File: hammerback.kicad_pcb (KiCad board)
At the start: 2 copper layers, 20.8 x 8.6 mm, 47 parts, among them J1 USB_C_Receptacle_USB2.0, P1 USB_C_Plug_USB2.0, U1 MCP73871, U2 TPS61090

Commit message: R0
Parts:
- removed BT1: Battery, KiCad/Connector_JST.pretty:JST_PH_S2B-PH-SM4-TB_1x02-1MP_P2.00mm_Horizontal
- removed F1: 3 A, KiCad/Capacitor_SMD.pretty:C_1206_3216Metric_Pad1.42x1.75mm_HandSolder
- removed REF** (x2): MountingHole_2.7mm_M2.5_ISO7380, KiCad/MountingHole.pretty:MountingHole_2.7mm_M2.5_ISO7380
- removed TH1: 10k, KiCad/Connector_PinHeader_2.54mm.pretty:PinHeader_1x02_P2.54mm_Vertical
- removed TP10, TP11, TP12, TP5, TP6, TP7, TP8, TP9: TestPoint, KiCad/TestPoint.pretty:TestPoint_Pad_D1.5mm
- added G***: LOGO, tunaf1sh/JBR-logos.pretty:hammerback, B.Cu at (155.3, 101.5)
- added G***: LOGO, tunaf1sh/JBR-logos.pretty:jbr-binary-xs-mask, B.Cu at (166.4, 100.2)
- added H1: MountingHole, KiCad/MountingHole.pretty:MountingHole_3.2mm_M3_ISO14580, F.Cu at (135.8, 95.7)
- added H2: MountingHole, KiCad/MountingHole.pretty:MountingHole_3.2mm_M3_ISO14580, F.Cu at (165.8, 95.7)
- added J2: LiPo, KiCad/Connector_PinHeader_2.54mm.pretty:PinHeader_1x03_P2.54mm_Vertical, F.Cu at (144.3, 97.7)
- JP1, R8, R9, TP3: moved to B.Cu
- TP1, TP2: value TestPoint_Probe -> TestPoint; footprint KiCad/TestPoint.pretty:TestPoint_Keystone_5019_Minature -> KiCad/TestPoint.pretty:TestPoint_Pad_D1.5mm
- moved C4 57.9 mm to (153.8, 98.7), turned to 180 degrees
- moved JP1 54.2 mm to (146.3, 101.7), turned to 90 degrees
- moved TP4 53.4 mm to (158.4, 98.3), turned to 90 degrees
- moved C1 51.5 mm to (146.6, 92.6)
- moved L1 50.2 mm to (155.3, 104.0), turned to 90 degrees
- moved TP3 45.7 mm to (150.9, 104.3)
- moved C5 44.7 mm to (166.7, 104.7)
- moved D1 44.7 mm to (144.3, 107.0)
- moved D2 44.7 mm to (142.6, 107.0)
- moved R1 44.7 mm to (148.9, 107.0)
- moved R10 44.7 mm to (141.1, 107.0)
- moved R2 44.7 mm to (147.4, 107.0)
- moved R7 44.7 mm to (145.8, 107.0)
- moved U1 44.6 mm to (148.3, 102.2)
- moved U2 44.4 mm to (162.0, 101.9), turned to 270 degrees
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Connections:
- net Net-(R5-Pad2) renamed /NTC
- TP1 pad 1: (no net) -> GND
- TP2 pad 1: GND -> VBUS
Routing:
- net GND: track 65.0 -> 114.0 mm, vias 6 -> 8
- net VBUS: track 7.46 -> 52.5 mm, vias 1 -> 4
- net /USB_N: track 4.81 -> 30.1 mm, vias 0 -> 3
- net /USB_P: track 7.58 -> 29.2 mm, vias 0 -> 3
- net VDD: track 15.4 -> 0.00 mm, vias 2 -> 0
- net Net-(BT1-Pad1): track 10.6 -> 0.00 mm
- net Net-(R16-Pad2): track 0.00 -> 9.82 mm
- net Net-(P1-PadB5): track 2.83 -> 12.0 mm
- net /NTC: track 4.63 -> 9.08 mm
- net Net-(P1-PadA5): track 4.49 -> 8.32 mm
- net Net-(C2-Pad1): track 29.5 -> 33.3 mm
- net Net-(C1-Pad1): track 24.3 -> 21.4 mm, vias 2 -> 1
- net Net-(J1-PadB5): track 0.00 -> 2.03 mm, vias 0 -> 1
- net Net-(J1-PadA5): track 0.00 -> 2.02 mm, vias 0 -> 1
- net +5V: track 30.1 -> 31.9 mm
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- added copper zone on B.Cu, net GND
- added copper zone on F.Cu, net GND
- removed copper zone on B.Cu, net (none)
- removed copper zone on F.Cu, net (none)
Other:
- board size 20.8 x 8.6 mm -> 36 x 18 mm
- board text added: "Hammerback R0 JBR Engineering 2021"
- board text removed: "+"
- board text removed: "-"
- board text removed: "2. VBATT- 1. VBATT+"
- board text removed: "5V"
- board text removed: "C1"
- board text removed: "C2"
- board text removed: "USB-C Plug"

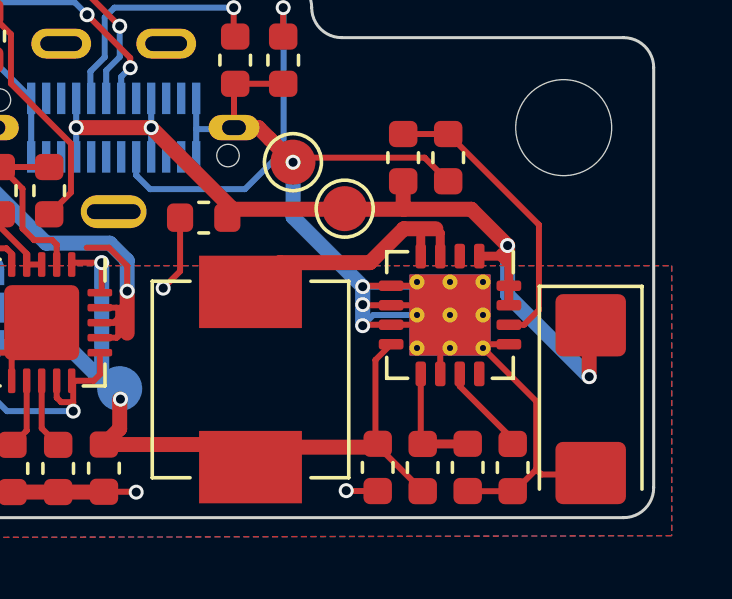
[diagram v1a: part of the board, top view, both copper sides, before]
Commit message: fix hole size in pad
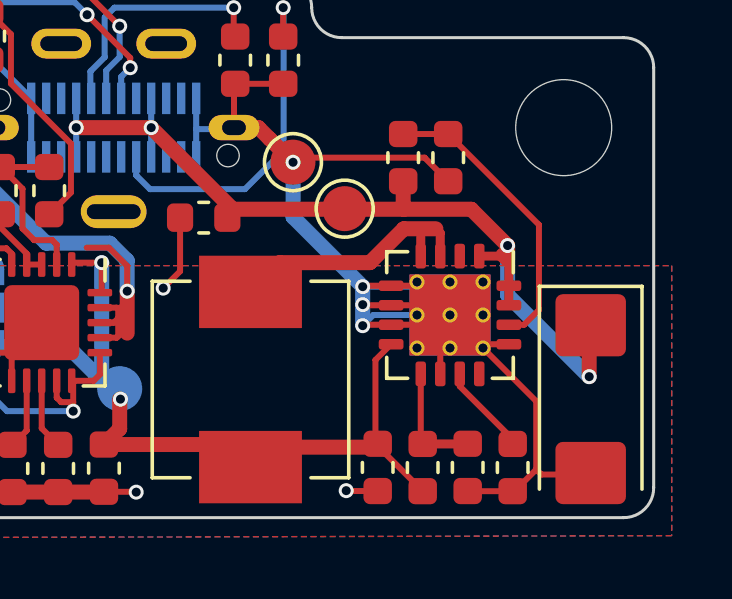
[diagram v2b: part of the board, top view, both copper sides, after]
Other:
- rule via_min_size: 0.5 -> 0.3
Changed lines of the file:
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@@
   )
   (setup
-    (last_trace_width 0.5)
+    (last_trace_width 0.2)
     (user_trace_width 0.3)
     (user_trace_width 0.5)
@@
     (via_size 0.5)
     (via_drill 0.3)
-    (via_min_size 0.5)
+    (via_min_size 0.3)
     (via_min_drill 0.3)
     (user_via 0.6 0.4)
@@
     (diff_pair_gap 0.15)
   )
-  (module KiCad/Capacitor_Tantalum_SMD.pretty:CP_EIA-6032-20_AVX-F (layer F.Cu)
-    (at 166.65 104.7 270)
-    (descr "Tantalum Capacitor SMD AVX-F (6032-20 Metric), IPC_7351 nominal, (Body size from: http://www.kemet.com/Lists/ProductCatalog/Attachments/253/KEM_TC101_STD.pdf), generated with kicad-footprint-generator")
-    (tags "capacitor tantalum")
-    (attr smd)
-    (fp_text reference C5 (at 0 -2.55 90) (layer F.SilkS) hide
-      (effects (font (size 1 1) (thickness 0.15)))
-    )
-    (fp_text value 100u (at 0 2.55 90) (layer F.Fab)
-      (effects (font (size 1 1) (thickness 0.15)))
-    )
-    (fp_line (start 3.75 1.85) (end -3.75 1.85) (layer F.CrtYd) (width 0.05))
-    (fp_line (start 3.75 -1.85) (end 3.75 1.85) (layer F.CrtYd) (width 0.05))
-    (fp_line (start -3.75 -1.85) (end 3.75 -1.85) (layer F.CrtYd) (width 0.05))
-    (fp_line (start -3.75 1.85) (end -3.75 -1.85) (layer F.CrtYd) (width 0.05))
-    (fp_line (start -3.76 1.71) (end 3 1.71) (layer F.SilkS) (width 0.12))
-    (fp_line (start -3.76 -1.71) (end -3.76 1.71) (layer F.SilkS) (width 0.12))
-    (fp_line (start 3 -1.71) (end -3.76 -1.71) (layer F.SilkS) (width 0.12))
-    (fp_line (start 3 1.6) (end 3 -1.6) (layer F.Fab) (width 0.1))
-    (fp_line (start -3 1.6) (end 3 1.6) (layer F.Fab) (width 0.1))
-    (fp_line (start -3 -0.8) (end -3 1.6) (layer F.Fab) (width 0.1))
-    (fp_line (start -2.2 -1.6) (end -3 -0.8) (layer F.Fab) (width 0.1))
-    (fp_line (start 3 -1.6) (end -2.2 -1.6) (layer F.Fab) (width 0.1))
-    (fp_text user %R (at 0 0 90) (layer F.Fab)
-      (effects (font (size 1 1) (thickness 0.15)))
-    )
-    (pad 2 smd roundrect (at 2.4625 0 270) (size 2.075 2.35) (layers F.Cu F.Paste F.Mask) (roundrect_rratio 0.1204819277108434)
-      (net 2 GND))
-    (pad 1 smd roundrect (at -2.4625 0 270) (size 2.075 2.35) (layers F.Cu F.Paste F.Mask) (roundrect_rratio 0.1204819277108434)
-      (net 5 +5V))
-    (model ${KISYS3DMOD}/Capacitor_Tantalum_SMD.3dshapes/CP_EIA-6032-20_AVX-F.wrl
-      (at (xyz 0 0 0))
-      (scale (xyz 1 1 1))
-      (rotate (xyz 0 0 0))
-    )
-  )
-  (module KiCad/MountingHole.pretty:MountingHole_3.2mm_M3_ISO14580 (layer F.Cu)
-    (at 165.75 95.65)
-    (descr "Mounting Hole 3.2mm, no annular, M3, ISO14580")
-    (tags "mounting hole 3.2mm no annular m3 iso14580")
-    (attr virtual)
-    (fp_text reference H2 (at 0 -3.75) (layer F.SilkS) hide
-      (effects (font (size 1 1) (thickness 0.15)))
-    )
-    (fp_text value MountingHole (at 0 3.75) (layer F.Fab)
-      (effects (font (size 1 1) (thickness 0.15)))
-    )
-    (fp_circle (center 0 0) (end 3 0) (layer F.CrtYd) (width 0.05))
-    (fp_circle (center 0 0) (end 2.75 0) (layer Cmts.User) (width 0.15))
-    (fp_text user %R (at 0.3 0) (layer F.Fab)
-      (effects (font (size 1 1) (thickness 0.15)))
-    )
-    (pad 1 np_thru_hole circle (at 0 0) (size 3.2 3.2) (drill 3.2) (layers *.Cu *.Mask))
-  )
   (module KiCad/Package_DFN_QFN.pretty:Texas_S-PVQFN-N16_EP2.7x2.7mm_ThermalVias (layer F.Cu)
     (at 161.96 101.895 270)
@@
     (tags "QFN NoLead")
     (attr smd)
-    (fp_text reference U2 (at 0 -3.32 90) (layer F.SilkS) hide
-      (effects (font (size 1 1) (thickness 0.15)))
-    )
-    (fp_text value TPS61090 (at 0 3.32 90) (layer F.Fab)
+    (fp_text reference U2 (at 0 -3.32 270) (layer F.SilkS) hide
+      (effects (font (size 1 1) (thickness 0.15)))
+    )
+    (fp_text value TPS61090 (at 0 3.32 270) (layer F.Fab)
       (effects (font (size 1 1) (thickness 0.15)))
     )
@@
     (fp_line (start 2.11 -2.11) (end 2.11 -1.41) (layer F.SilkS) (width 0.12))
     (fp_line (start 1.41 -2.11) (end 2.11 -2.11) (layer F.SilkS) (width 0.12))
-    (fp_text user %R (at 0 0 90) (layer F.Fab)
+    (fp_text user %R (at 0 0 270) (layer F.Fab)
       (effects (font (size 1 1) (thickness 0.15)))
     )
@@
     (pad 17 smd rect (at 0 0 270) (size 2.7 2.7) (layers B.Cu)
       (net 2 GND))
-    (pad 17 thru_hole circle (at 1.1 1.1 270) (size 0.5 0.5) (drill 0.2) (layers *.Cu)
-      (net 2 GND))
-    (pad 17 thru_hole circle (at 0 1.1 270) (size 0.5 0.5) (drill 0.2) (layers *.Cu)
-      (net 2 GND))
-    (pad 17 thru_hole circle (at -1.1 1.1 270) (size 0.5 0.5) (drill 0.2) (layers *.Cu)
-      (net 2 GND))
-    (pad 17 thru_hole circle (at 1.1 0 270) (size 0.5 0.5) (drill 0.2) (layers *.Cu)
-      (net 2 GND))
-    (pad 17 thru_hole circle (at 0 0 270) (size 0.5 0.5) (drill 0.2) (layers *.Cu)
-      (net 2 GND))
-    (pad 17 thru_hole circle (at -1.1 0 270) (size 0.5 0.5) (drill 0.2) (layers *.Cu)
-      (net 2 GND))
-    (pad 17 thru_hole circle (at 1.1 -1.1 270) (size 0.5 0.5) (drill 0.2) (layers *.Cu)
-      (net 2 GND))
-    (pad 17 thru_hole circle (at 0 -1.1 270) (size 0.5 0.5) (drill 0.2) (layers *.Cu)
-      (net 2 GND))
-    (pad 17 thru_hole circle (at -1.1 -1.1 270) (size 0.5 0.5) (drill 0.2) (layers *.Cu)
+    (pad 17 thru_hole circle (at 1.1 1.1 270) (size 0.5 0.5) (drill 0.3) (layers *.Cu)
+      (net 2 GND))
+    (pad 17 thru_hole circle (at 0 1.1 270) (size 0.5 0.5) (drill 0.3) (layers *.Cu)
+      (net 2 GND))
+    (pad 17 thru_hole circle (at -1.1 1.1 270) (size 0.5 0.5) (drill 0.3) (layers *.Cu)
+      (net 2 GND))
+    (pad 17 thru_hole circle (at 1.1 0 270) (size 0.5 0.5) (drill 0.3) (layers *.Cu)
+      (net 2 GND))
+    (pad 17 thru_hole circle (at 0 0 270) (size 0.5 0.5) (drill 0.3) (layers *.Cu)
+      (net 2 GND))
+    (pad 17 thru_hole circle (at -1.1 0 270) (size 0.5 0.5) (drill 0.3) (layers *.Cu)
+      (net 2 GND))
+    (pad 17 thru_hole circle (at 1.1 -1.1 270) (size 0.5 0.5) (drill 0.3) (layers *.Cu)
+      (net 2 GND))
+    (pad 17 thru_hole circle (at 0 -1.1 270) (size 0.5 0.5) (drill 0.3) (layers *.Cu)
+      (net 2 GND))
+    (pad 17 thru_hole circle (at -1.1 -1.1 270) (size 0.5 0.5) (drill 0.3) (layers *.Cu)
       (net 2 GND))
     (pad 17 smd rect (at 0 0 270) (size 2.7 2.7) (layers F.Cu F.Mask)
@@
     )
   )
+  (module KiCad/Capacitor_Tantalum_SMD.pretty:CP_EIA-6032-20_AVX-F (layer F.Cu)
+    (at 166.65 104.7 270)
+    (descr "Tantalum Capacitor SMD AVX-F (6032-20 Metric), IPC_7351 nominal, (Body size from: http://www.kemet.com/Lists/ProductCatalog/Attachments/253/KEM_TC101_STD.pdf), generated with kicad-footprint-generator")
+    (tags "capacitor tantalum")
+    (attr smd)
+    (fp_text reference C5 (at 0 -2.55 90) (layer F.SilkS) hide
+      (effects (font (size 1 1) (thickness 0.15)))
+    )
+    (fp_text value 100u (at 0 2.55 90) (layer F.Fab)
+      (effects (font (size 1 1) (thickness 0.15)))
+    )
+    (fp_line (start 3.75 1.85) (end -3.75 1.85) (layer F.CrtYd) (width 0.05))
+    (fp_line (start 3.75 -1.85) (end 3.75 1.85) (layer F.CrtYd) (width 0.05))
+    (fp_line (start -3.75 -1.85) (end 3.75 -1.85) (layer F.CrtYd) (width 0.05))
+    (fp_line (start -3.75 1.85) (end -3.75 -1.85) (layer F.CrtYd) (width 0.05))
+    (fp_line (start -3.76 1.71) (end 3 1.71) (layer F.SilkS) (width 0.12))
+    (fp_line (start -3.76 -1.71) (end -3.76 1.71) (layer F.SilkS) (width 0.12))
+    (fp_line (start 3 -1.71) (end -3.76 -1.71) (layer F.SilkS) (width 0.12))
+    (fp_line (start 3 1.6) (end 3 -1.6) (layer F.Fab) (width 0.1))
+    (fp_line (start -3 1.6) (end 3 1.6) (layer F.Fab) (width 0.1))
+    (fp_line (start -3 -0.8) (end -3 1.6) (layer F.Fab) (width 0.1))
+    (fp_line (start -2.2 -1.6) (end -3 -0.8) (layer F.Fab) (width 0.1))
+    (fp_line (start 3 -1.6) (end -2.2 -1.6) (layer F.Fab) (width 0.1))
+    (fp_text user %R (at 0 0 90) (layer F.Fab)
+      (effects (font (size 1 1) (thickness 0.15)))
+    )
+    (pad 2 smd roundrect (at 2.4625 0 270) (size 2.075 2.35) (layers F.Cu F.Paste F.Mask) (roundrect_rratio 0.1204819277108434)
+      (net 2 GND))
+    (pad 1 smd roundrect (at -2.4625 0 270) (size 2.075 2.35) (layers F.Cu F.Paste F.Mask) (roundrect_rratio 0.1204819277108434)
+      (net 5 +5V))
+    (model ${KISYS3DMOD}/Capacitor_Tantalum_SMD.3dshapes/CP_EIA-6032-20_AVX-F.wrl
+      (at (xyz 0 0 0))
+      (scale (xyz 1 1 1))
+      (rotate (xyz 0 0 0))
+    )
+  )
+  (module KiCad/MountingHole.pretty:MountingHole_3.2mm_M3_ISO14580 (layer F.Cu)
+    (at 165.75 95.65)
+    (descr "Mounting Hole 3.2mm, no annular, M3, ISO14580")
+    (tags "mounting hole 3.2mm no annular m3 iso14580")
+    (attr virtual)
+    (fp_text reference H2 (at 0 -3.75) (layer F.SilkS) hide
+      (effects (font (size 1 1) (thickness 0.15)))
+    )
+    (fp_text value MountingHole (at 0 3.75) (layer F.Fab)
+      (effects (font (size 1 1) (thickness 0.15)))
+    )
+    (fp_circle (center 0 0) (end 3 0) (layer F.CrtYd) (width 0.05))
+    (fp_circle (center 0 0) (end 2.75 0) (layer Cmts.User) (width 0.15))
+    (fp_text user %R (at 0.3 0) (layer F.Fab)
+      (effects (font (size 1 1) (thickness 0.15)))
+    )
+    (pad 1 np_thru_hole circle (at 0 0) (size 3.2 3.2) (drill 3.2) (layers *.Cu *.Mask))
+  )
   (module tunaf1sh/JBR-logos.pretty:hammerback (layer B.Cu)

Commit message: pcb updates
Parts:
- added JP2: SolderJumper_2_Open, KiCad/Jumper.pretty:SolderJumper-2_P1.3mm_Open_RoundedPad1.0x1.5mm, B.Cu at (163.5, 104.8)
- R14, R15, R8, R9: value 5k9 -> 5k1
- renumbered J1 to ee1
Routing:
- net Net-(C2-Pad1): track 33.3 -> 36.7 mm, vias 2 -> 3
- net /BOOST: track 3.09 -> 3.99 mm, vias 0 -> 1

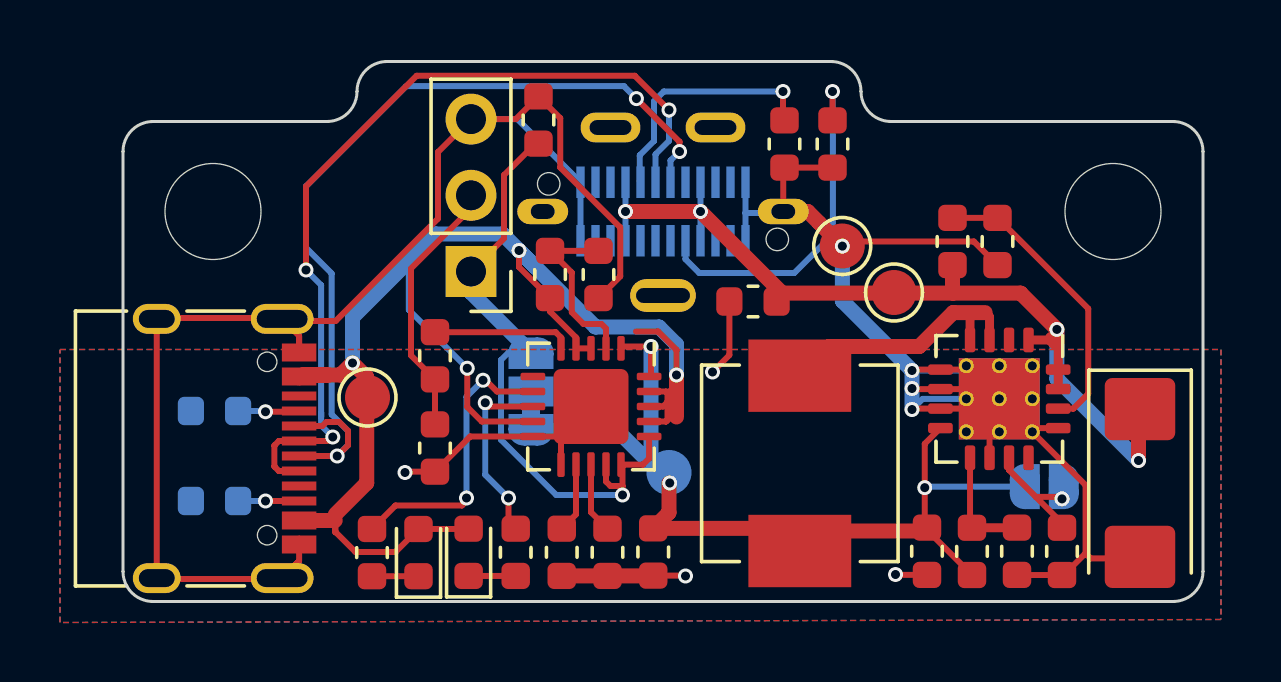
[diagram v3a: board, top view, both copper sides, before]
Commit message: update for kicad 7
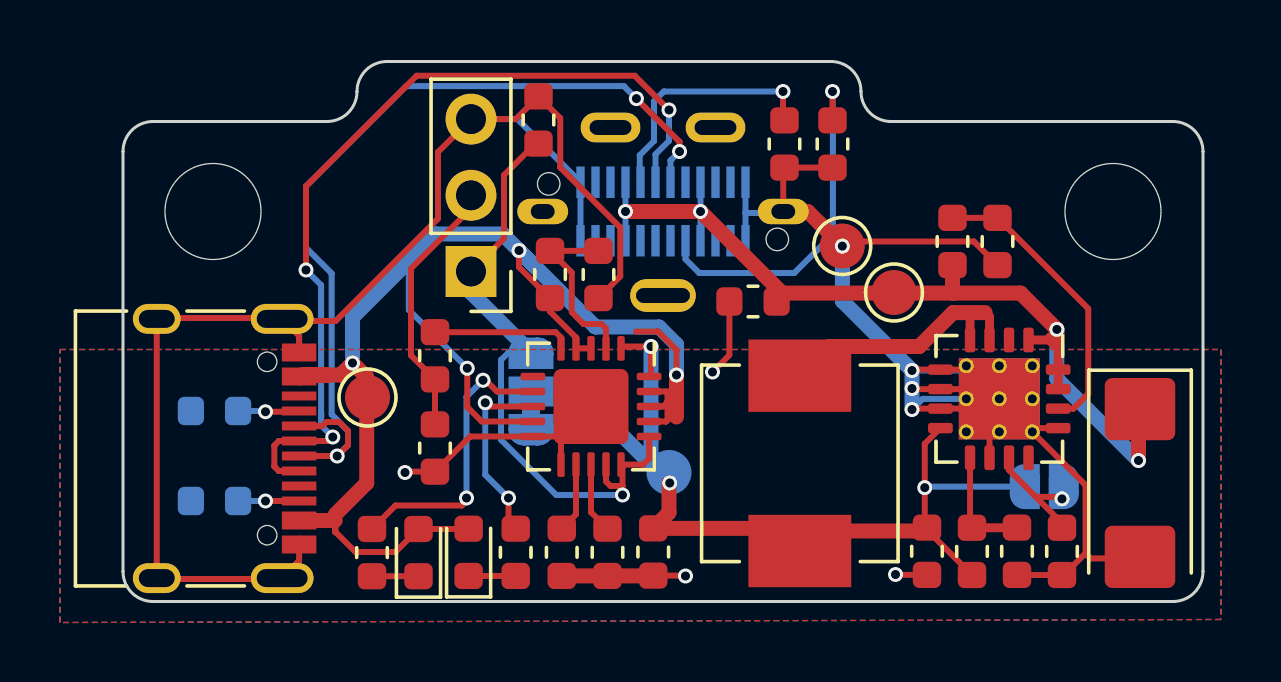
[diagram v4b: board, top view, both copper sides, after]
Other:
- net class Default removed
- net class VBUS removed
